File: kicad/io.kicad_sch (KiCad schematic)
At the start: 5 parts, among them U10 74AC138, U11 SC16C752, U12 W65C22S

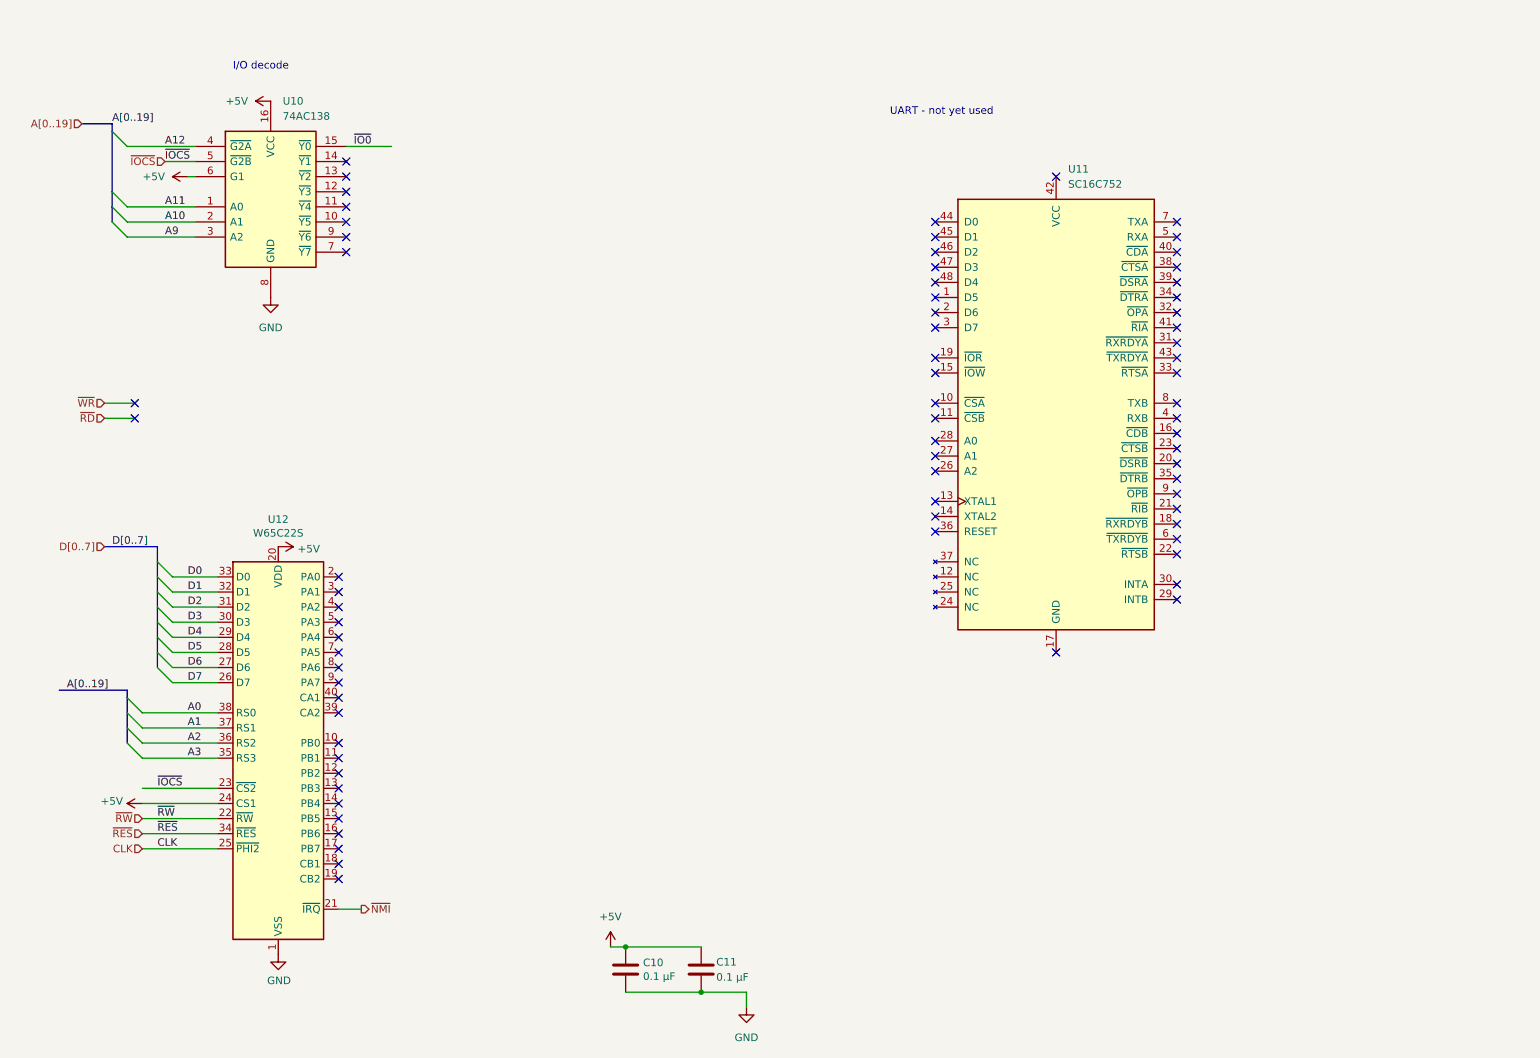
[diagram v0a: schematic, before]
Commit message: connect UART to circuit
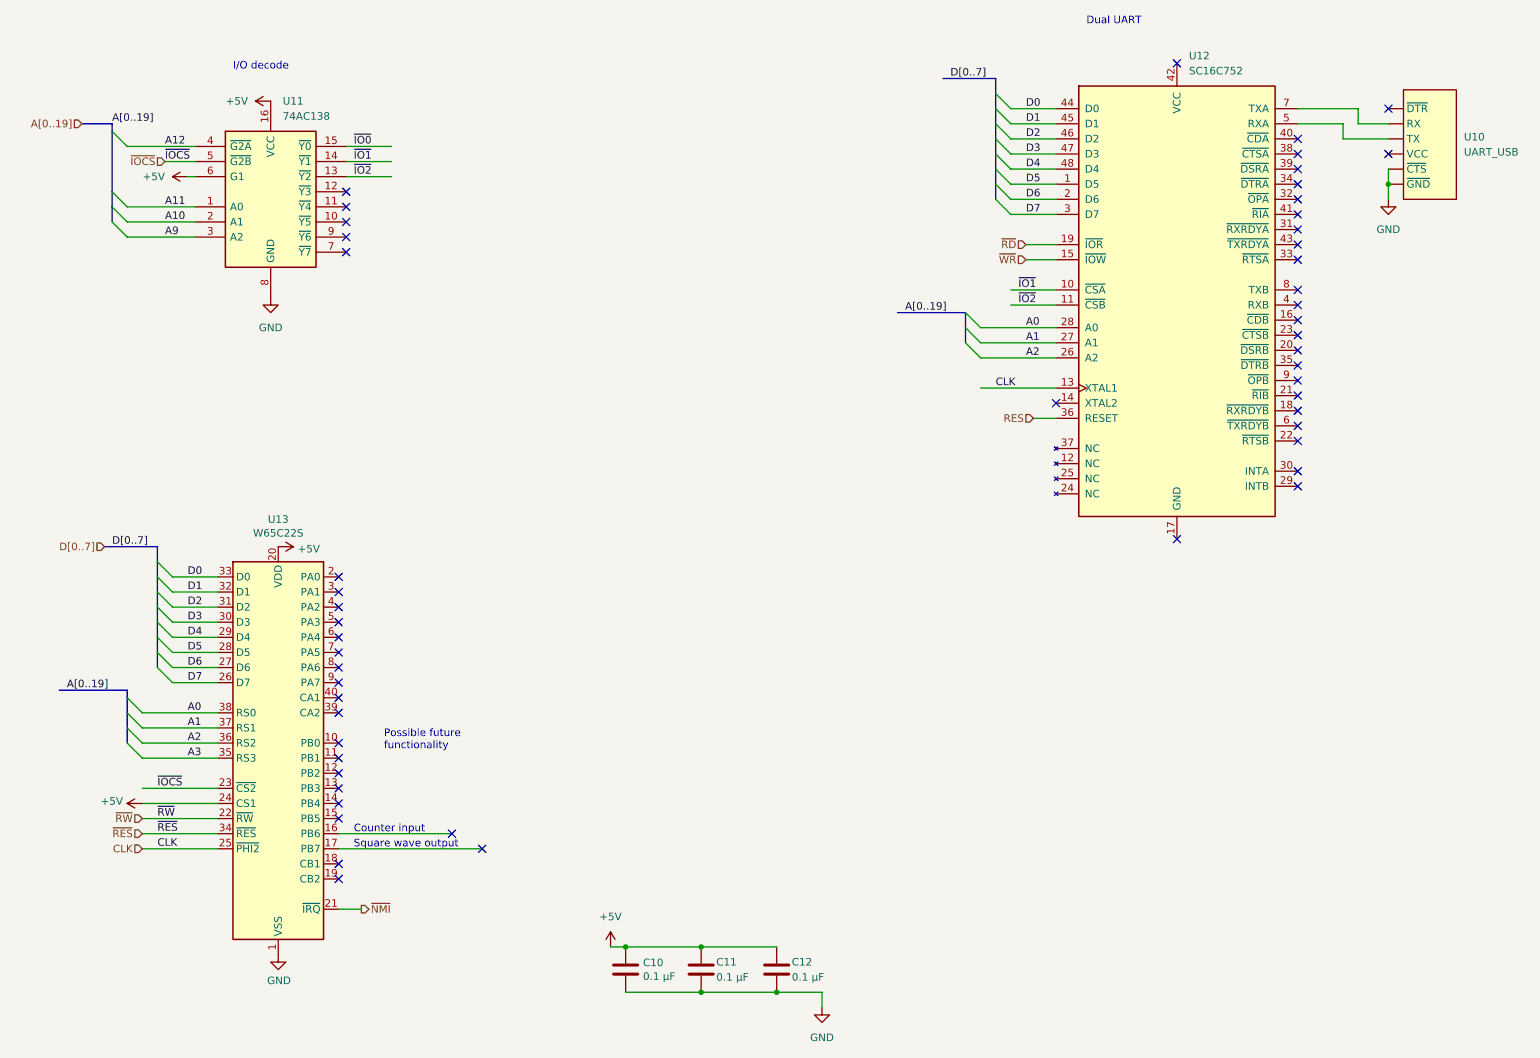
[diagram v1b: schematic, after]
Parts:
- added C12: 0.1 µF, symbol Device:C
- added U10: UART_USB, symbol project:UART_USB
- renumbered U10 to U11, U11 to U12, U12 to U13
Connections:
- net +5V: now also C12.1
- net A0: now also U12.28 (A0)
- net A1: now also U12.27 (A1)
- net A2: now also U12.26 (A2)
- net CLK: now also U12.13 (XTAL1)
- net D0: now also U12.44 (D0)
- net D1: now also U12.45 (D1)
- net D2: now also U12.46 (D2)
- net D3: now also U12.47 (D3)
- net D4: now also U12.48 (D4)
- net D5: now also U12.1 (D5)
- net D6: now also U12.2 (D6)
- net D7: now also U12.3 (D7)
- net GND: now also C12.2, U10. (~{GND})
- net ~{RD}: now also U12.19 (~{IOR})
- net ~{WR}: now also U12.15 (~{IOW})
- net ~{IO1}: now reaches U12.10 (~{CSA})
- net ~{IO1}: now also U11.14 (~{Y1})
- net ~{IO2}: now reaches U12.11 (~{CSB})
- net ~{IO2}: now also U11.13 (~{Y2})
- net RES: now reaches U12.36 (RESET)
- net at U12.5 (RXA): now also U10. (~{GND})
- net at U12.7 (TXA): now also U10. (~{GND})
- no-connect marks 73 -> 52
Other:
- note added: "Counter input"
- note added: "Dual UART"
- note added: "Possible future functionality"
- note added: "Square wave output"
- note removed: "UART - not yet used"
- moved on the sheet: U12
